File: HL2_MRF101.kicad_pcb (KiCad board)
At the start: 4 copper layers, 149.9 x 100 mm, 224 parts, among them J1 Antenna, J10 DB1, J2 HL2, J3 RF3, J4 RF1, J5 RCJ-041, J6 50VDC, J7 12V, J8 Fan, J9 HL2_12V, K1 EC2-3NU, K10 EC2-3NU, K11 EC2-3NU, K12 EC2-3NU, K13 EC2-3NU, K2 EC2-3NU, K3 EC2-3NU, K4 EC2-3NU, K5 EC2-3NU, K6 EC2-3NU, K7 EC2-3NU, K8 EC2-3NU, K9 EC2-3NU, Q1 MRF101AN, Q2 2N7002, Q3 IRLML6402, Q4 DTC144E, T1 Coupler, T2 Coupler, T3 744851330, U1 MCP6282E/MS, U2 MAX11613, U3 MCP23008, U4 ULN2003, U5 LM35-NEB, U6 MCP4561, U7 INA193

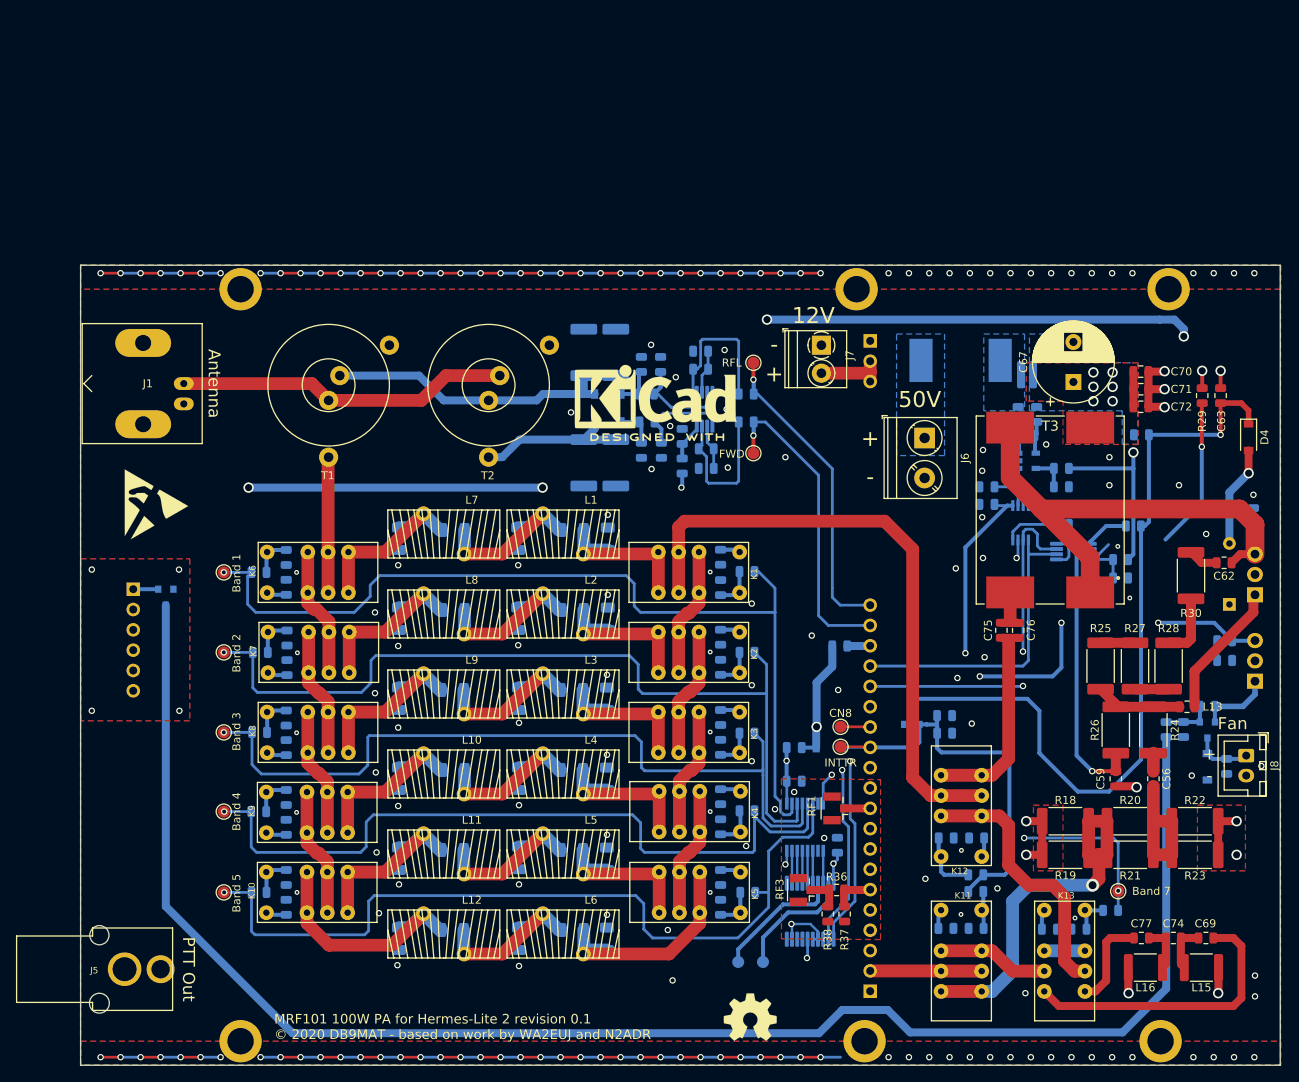
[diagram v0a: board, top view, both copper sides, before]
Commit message: Almost finished reworking FET part
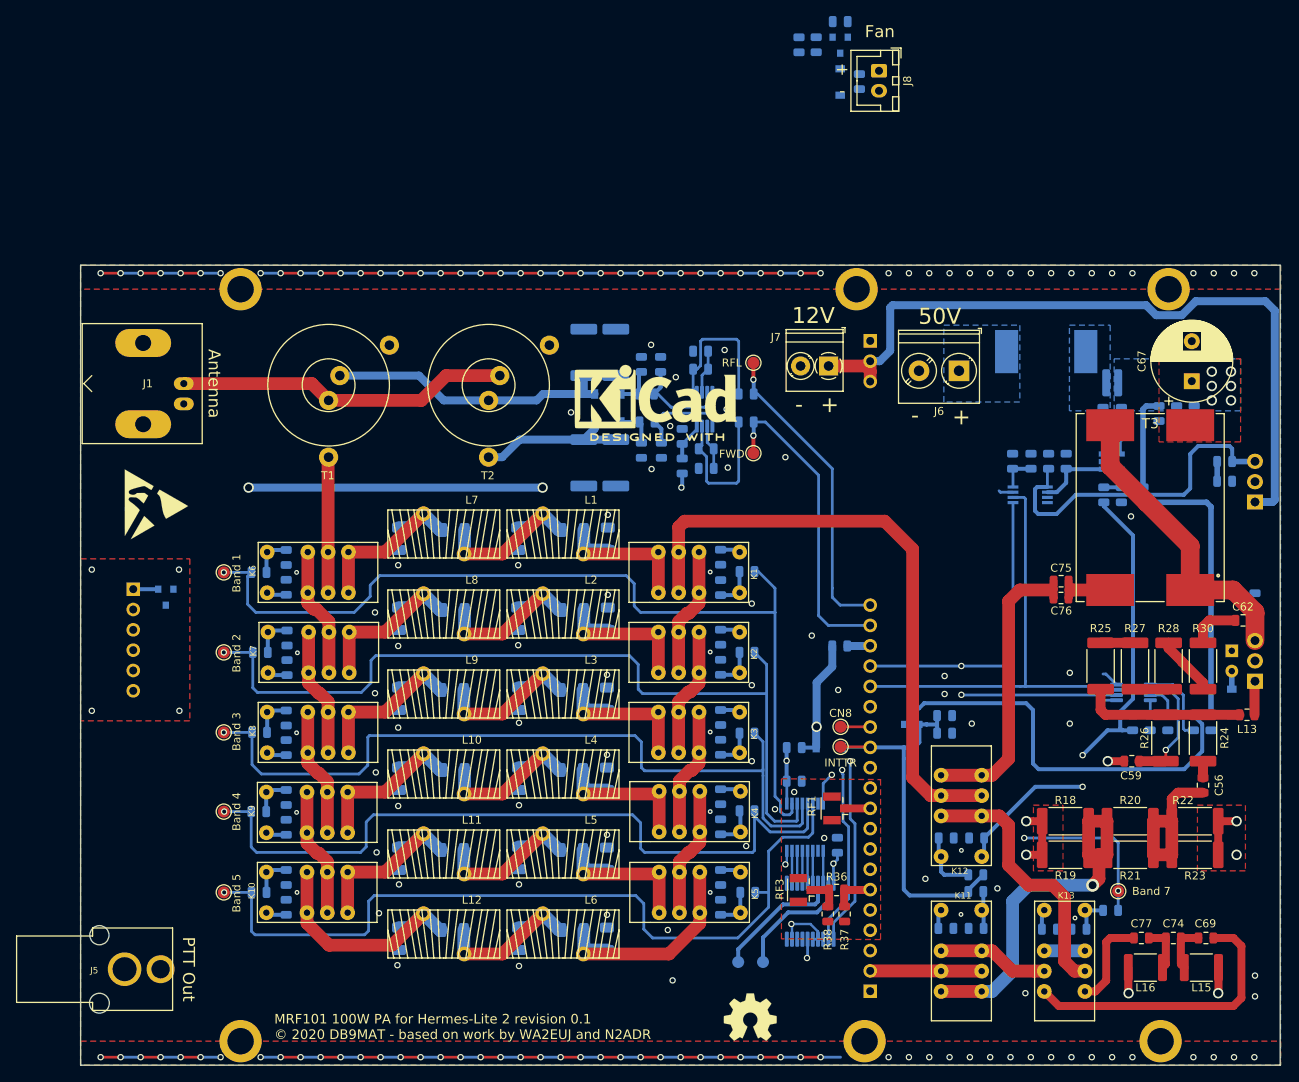
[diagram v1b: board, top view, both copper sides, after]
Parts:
- C63, C70, C71, C72, D4, R29: moved to B.Cu
- D5: footprint Diode_THT:D_DO-35_SOD27_P7.62mm_Horizontal -> Diode_THT:D_DO-35_SOD27_P2.54mm_Vertical_KathodeUp
- moved C85 97.1 mm to (167.3, 17.1)
- moved R16 97.1 mm to (164.9, 9.55)
- moved C84 97.1 mm to (161.9, 12.4)
- moved D6 97.1 mm to (164.9, 17.1)
- moved Q3 97.1 mm to (164.9, 12.5)
- moved J8 97.1 mm to (169.8, 15.7)
- moved R17 97.1 mm to (159.8, 12.4)
- moved R29 41.1 mm to (205.9, 97.2), turned to 90 degrees
- moved C63 40.9 mm to (211.3, 97.2), turned to 90 degrees
- moved D4 33.2 mm to (213.9, 94.7), turned to 90 degrees
- moved R39 25.7 mm to (209.1, 97.2), turned to 270 degrees
- moved C61 22.4 mm to (213.0, 67.0)
- moved U5 22.4 mm to (216.8, 69.6)
- moved R33 22.4 mm to (213.0, 64.5)
- moved FB7 20.5 mm to (201.5, 97.2), turned to 270 degrees
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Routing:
- net Net-(Q4-Pad3): track 205.3 -> 0.00 mm
- net +3V3: track 536.7 -> 459.4 mm, vias 9 -> 8
- net +12V: track 18.0 -> 92.6 mm
- net Vtemp: track 68.6 -> 42.1 mm, vias 4 -> 0
- net SCL: track 75.2 -> 97.3 mm, vias 1 -> 3
- net Net-(C62-Pad1): track 63.0 -> 41.6 mm
- net GND: track 236.2 -> 215.1 mm, vias 204 -> 186
- net Net-(C59-Pad1): track 35.3 -> 15.7 mm
- net Net-(R29-Pad2): track 21.8 -> 4.30 mm, vias 1 -> 0
- net Net-(L13-Pad2): track 17.0 -> 4.23 mm
- net SDA: track 79.9 -> 91.4 mm, vias 3 -> 1
- net TX_high: track 26.1 -> 36.8 mm
- net Net-(D4-Pad2): track 12.6 -> 2.26 mm, vias 1 -> 0
- net Net-(C63-Pad2): track 99.1 -> 89.4 mm, vias 1 -> 0
- net Net-(L13-Pad1): track 10.9 -> 20.2 mm
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
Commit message: Updated FET circuit
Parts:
- R10, R5: value 56k -> 100k
- R11, R4: value 100k -> 56k
- U2: value MAX11613 -> MAX11645
- moved J8 137.4 mm to (74.2, 114.4), turned to 90 degrees
- moved C85 131.9 mm to (76.8, 113.0)
- moved R16 130.4 mm to (76.1, 105.1), turned to 90 degrees
- moved Q3 130.4 mm to (73.2, 105.1), turned to 180 degrees
- moved D6 128.6 mm to (79.2, 112.9)
- moved C84 126.1 mm to (73.2, 102.1), turned to 0 degrees
- moved R17 123.1 mm to (73.2, 99.9), turned to 180 degrees
- moved Q4 17.2 mm to (73.2, 97.0)
- moved C78 2.30 mm to (186.5, 64.5)
- moved FB4 2.30 mm to (188.8, 64.5), turned to 90 degrees
- moved U2 0.33 mm to (188.7, 69.0)
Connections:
- C79 pad 2: Vipa -> Vtemp
- C80 pad 2: Vtemp -> Vipa
- U2 pad 1: Vtemp -> Vipa
- U2 pad 2: Vipa -> Vtemp
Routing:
- net +12V: track 92.6 -> 263.5 mm
- net Net-(J10-Pad1): track 3.12 -> 18.1 mm
- net +3V3: track 459.4 -> 474.3 mm
- net Net-(C85-Pad2): track 0.00 -> 13.9 mm
- net GND: track 215.1 -> 226.5 mm, vias 186 -> 200
- net Net-(C84-Pad2): track 0.00 -> 6.16 mm
- net Vtemp: track 42.1 -> 36.0 mm
- net Net-(Q4-Pad3): track 0.00 -> 2.27 mm
- net Vipa: track 9.30 -> 11.0 mm
- net Net-(C78-Pad2): track 4.56 -> 5.71 mm
- net SDA: track 91.4 -> 90.8 mm
- net Net-(C63-Pad2): track 89.4 -> 88.8 mm

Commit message: Revision 0.2
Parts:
- removed the REF** at (141.9, 56.4)
- added G***: LOGO, n2adr:Ham_Logo, F.Cu at (139.4, 56.2)
- Q3, Q4: footprint TO_SOT_Packages_SMD:SOT-23 -> Package_TO_SOT_SMD:SOT-23
- moved C42 3.16 mm to (94.7, 119.5)
- moved C53 3.16 mm to (94.7, 123.3)
- moved FB18 3.16 mm to (91.3, 121.4)
- moved K10 3.16 mm to (97.3, 121.4)
- moved TP12 3.16 mm to (86.9, 121.4)
- moved C30 3.13 mm to (115.6, 126.1)
- moved L12 3.13 mm to (114.5, 126.6)
- moved C36 3.13 mm to (108.9, 127.2)
- moved C11 3.00 mm to (135.8, 127.2)
- moved C17 3.00 mm to (131.5, 126.1)
- moved C24 3.00 mm to (124.8, 127.2)
- moved L6 3.00 mm to (130.3, 126.6)
- moved C52 2.90 mm to (150.0, 119.4)
- moved C5 2.90 mm to (150.0, 123.2)
- moved FB17 2.90 mm to (153.4, 121.3)
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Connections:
- C79 pad 2: Vtemp -> Vipa
- C80 pad 2: Vipa -> Vtemp
- U2 pad 1: Vipa -> Vtemp
- U2 pad 2: Vtemp -> Vipa
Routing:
- net +3V3: track 474.3 -> 486.2 mm, vias 8 -> 7
- net Band2: track 107.0 -> 111.6 mm
- net Band1: track 114.7 -> 117.8 mm
- net Band3: track 98.6 -> 101.6 mm
- net Vipa: track 11.0 -> 13.1 mm
- net Band5: track 101.8 -> 103.5 mm
- net Net-(TP5-Pad1): track 16.3 -> 17.8 mm
- net Net-(TP2-Pad1): track 15.3 -> 16.7 mm
- net Net-(C63-Pad2): track 88.8 -> 89.9 mm
- net Net-(C16-Pad2): track 21.6 -> 22.5 mm
- net Net-(D2-Pad2): track 39.8 -> 40.7 mm
- net Net-(D1-Pad2): track 19.6 -> 20.5 mm
- net Net-(C13-Pad2): track 21.9 -> 22.8 mm
- net Net-(J1-Pad1): track 41.7 -> 40.8 mm
- net Net-(C17-Pad2): track 21.8 -> 22.7 mm
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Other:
- board text added: "MRF101 100W PA for Hermes-Lite 2 revision 0.2 © 2020 DB9MAT - based on work by WA2EUJ and N2ADR"
- board text removed: "JLCJLCJLCJLC"
- board text removed: "MRF101 100W PA for Hermes-Lite 2 revision 0.1 © 2020 DB9MAT - based on work by WA2EUJ and N2ADR"

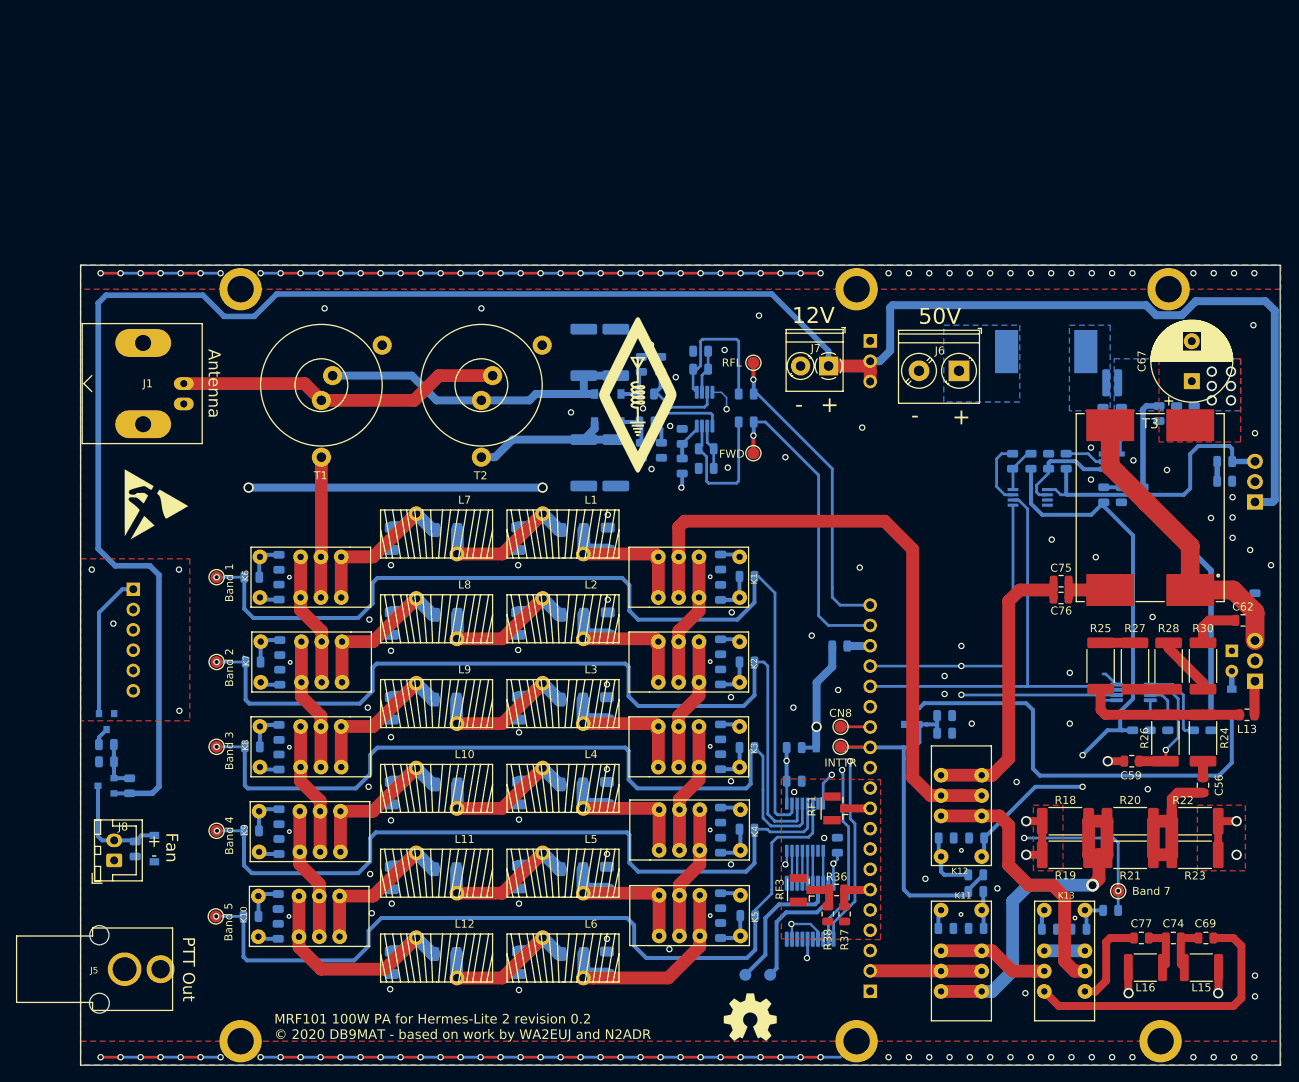
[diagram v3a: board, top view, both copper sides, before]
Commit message: Rx antenna change
RX antenna routed through HL2 rx antenna connection. High power tx tracks thickened to 2 mm and net list added for 50 ohm impedance top and bottom tracks for clearance.
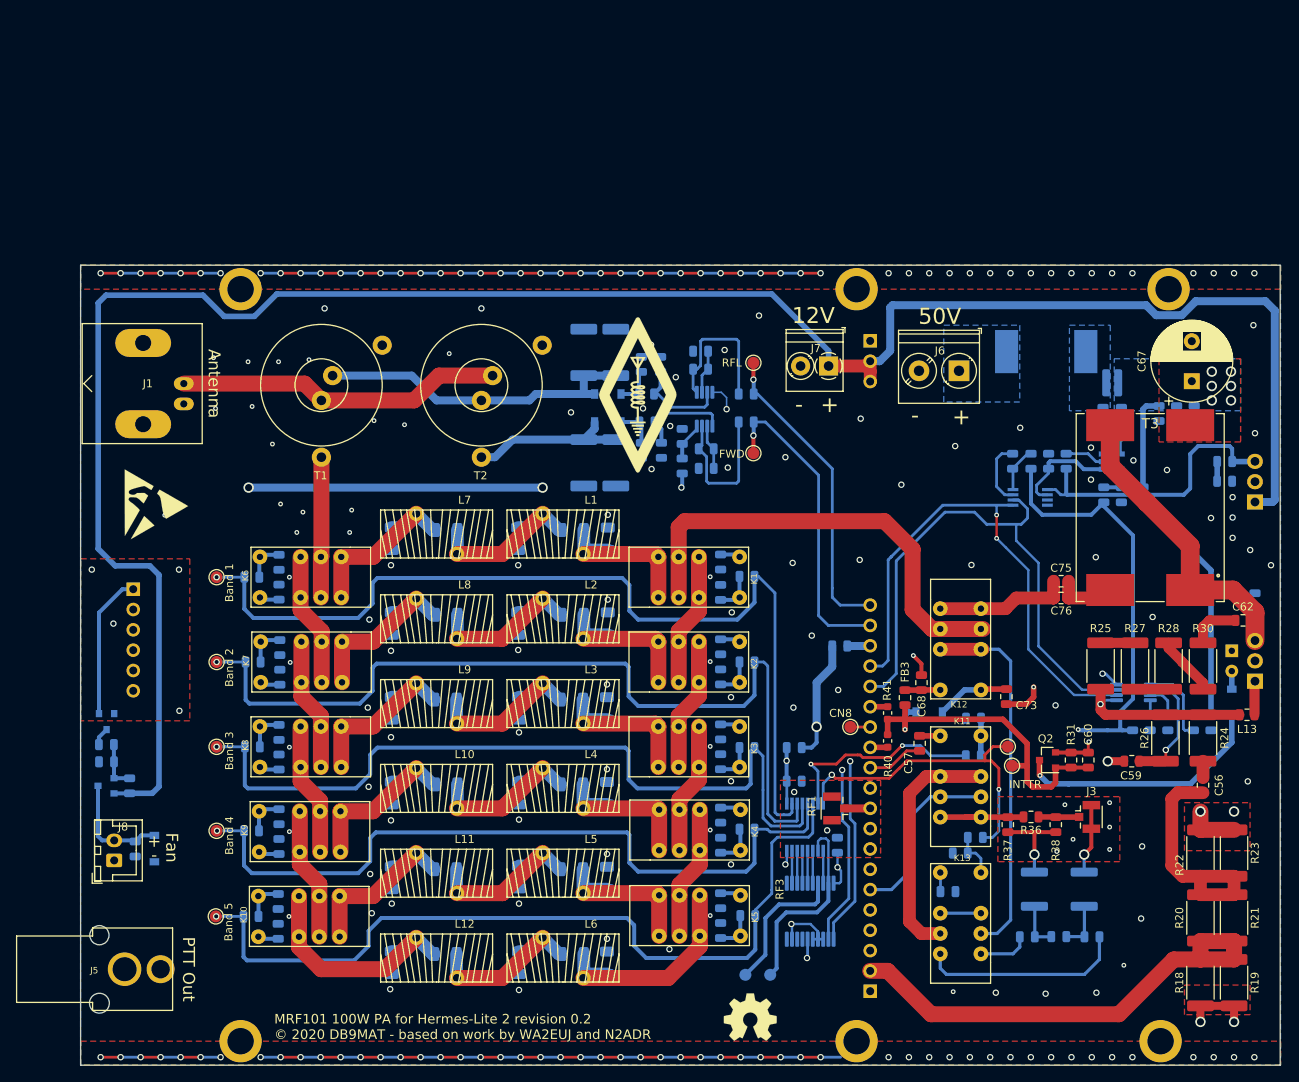
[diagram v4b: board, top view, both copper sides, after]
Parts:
- added R40: 0R, Resistor_SMD:R_0603_1608Metric, F.Cu at (170.9, 99.5)
- added R41: 0R, Resistor_SMD:R_0603_1608Metric, F.Cu at (170.9, 96.0)
- C57, C60, C68, C73, FB3, Q2, R31: moved to F.Cu
- C69, C74, C77, L15, L16: moved to B.Cu
- J3: footprint Connector_Coaxial:U.FL_Hirose_U.FL-R-SMT-1_Vertical -> n2adr:U.FL_Hirose_U.FL-R-SMT-1_Vertical
- moved J3 36.8 mm to (195.9, 109.0), turned to 0 degrees
- moved R38 30.6 mm to (191.9, 109.9)
- moved R19 26.5 mm to (214.2, 129.7), turned to 90 degrees
- moved R18 26.3 mm to (210.0, 129.7), turned to 90 degrees
- moved C58 26.3 mm to (181.6, 96.6)
- moved R36 26.0 mm to (188.8, 109.0), turned to 180 degrees
- moved FB3 23.8 mm to (173.1, 94.1), turned to 90 degrees
- moved C57 23.4 mm to (174.9, 99.8), turned to 270 degrees
- moved R37 23.3 mm to (185.9, 109.9)
- moved TP14 22.7 mm to (185.9, 100.2)
- moved K11 21.8 mm to (180.0, 103.9)
- moved TP7 21.6 mm to (186.4, 102.6)
- moved K12 20.8 mm to (180.0, 88.0)
- moved C68 19.7 mm to (175.1, 92.2), turned to 90 degrees
- moved FB19 19.2 mm to (181.8, 111.5)
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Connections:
- FB2 pad 2: INTTR -> RXANT
- J2 pad 13: INTTR -> Net-(J2-Pad13)
- J2 pad 6: Net-(J2-Pad6) -> HL2_RX
- K11 pad 3: HL2_RF -> HL2_RX
- K11 pad 4: HL2_TX -> Net-(K11-Pad4)
- K11 pad 5: HL2_TX -> Net-(K11-Pad4)
- K11 pad 6: HL2_RF -> HL2_RX
- R18 pad 2: HL2_TX -> HL2_RF
- R19 pad 2: HL2_TX -> HL2_RF
- R20 pad 1: HL2_TX -> HL2_RF
- R21 pad 2: HL2_TX -> HL2_RF
- R36 pad 2: Net-(J2-Pad6) -> Net-(K11-Pad4)
- R37 pad 2: Net-(J2-Pad6) -> Net-(K11-Pad4)
- U4 pad 15: Net-(U4-Pad15) -> RXANT
- U4 pad 2: Net-(U4-Pad2) -> Net-(TP2-Pad1)
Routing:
- net HL2_TX: track 46.7 -> 0.00 mm, vias 1 -> 0
- net HL2_RF: track 14.0 -> 59.4 mm
- net GND: track 226.5 -> 260.3 mm, vias 208 -> 232
- net RXANT: track 0.00 -> 26.4 mm, vias 0 -> 2
- net Net-(C63-Pad2): track 89.9 -> 66.8 mm, vias 0 -> 1
- net HL2_RX: track 0.00 -> 22.7 mm
- net Filter_In: track 77.9 -> 57.2 mm
- net TX_high: track 36.8 -> 16.8 mm
- net Net-(K11-Pad2): track 14.0 -> 30.3 mm
- net SDA: track 90.8 -> 105.1 mm
- net Band7: track 53.3 -> 40.6 mm, vias 3 -> 2
- net Net-(K12-Pad2): track 33.6 -> 46.2 mm
- net Net-(K11-Pad4): track 0.00 -> 12.3 mm
- net Net-(C69-Pad2): track 36.2 -> 25.7 mm
- net Net-(C56-Pad2): track 20.0 -> 29.7 mm
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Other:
- net class 50z_bottom added: clearance 0.5, trace_width 0.4, via_dia 0.6, via_drill 0.3
- net class 50z_top added: clearance 0.5, trace_width 2, via_dia 0.6, via_drill 0.3

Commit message: Update relays
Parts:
- removed the REF** at (153.7, 134.0) (x2)
- removed TP10, TP11, TP12, TP14, TP2, TP8, TP9: P8, TestPoint:TestPoint_Pad_D1.5mm
- added REF**: OSHW-Symbol_6.7x6mm_SilkScreen, Symbol:OSHW-Symbol_6.7x6mm_SilkScreen, B.Cu at (161.0, 133.9)
- added REF**: OSHW-Symbol_6.7x6mm_SilkScreen, Symbol:OSHW-Symbol_6.7x6mm_SilkScreen, F.Cu at (161.2, 133.3)
- C55, D3, FB5: moved to F.Cu
- J10: footprint Connector_PinSocket_2.54mm:PinSocket_1x06_P2.54mm_Vertical -> Connector_PinHeader_2.54mm:PinHeader_1x06_P2.54mm_Vertical
- J4: footprint Connector_Coaxial:U.FL_Hirose_U.FL-R-SMT-1_Vertical -> n2adr:U.FL_Hirose_U.FL-R-SMT-1_Vertical
- K1, K10, K12, K2, K3, K4, K5, K6, K7, K8, K9: value EC2-3NU -> AXICOM D2N; footprint n2adr:RelayDPDT01 -> n2adr:RelayDPDT02
- moved D3 15.7 mm to (191.6, 98.0)
- moved TP5 11.4 mm to (164.5, 129.5)
- moved FB5 7.75 mm to (159.8, 108.0), turned to 90 degrees
- moved C53 7.68 mm to (88.1, 127.3)
- moved C38 7.37 mm to (87.9, 74.6)
- moved C51 7.30 mm to (88.1, 115.6)
- moved C39 7.18 mm to (87.9, 86.3)
- moved C46 7.04 mm to (87.9, 92.1)
- moved C44 6.93 mm to (87.9, 80.4)
- moved C42 6.87 mm to (88.1, 121.6)
- moved C49 6.85 mm to (88.1, 103.7)
- moved C41 6.73 mm to (88.1, 109.9)
- moved C40 6.68 mm to (88.1, 98.0)
- moved FB17 6.29 mm to (154.4, 127.5), turned to 90 degrees
- moved FB15 5.27 mm to (154.4, 115.6), turned to 90 degrees
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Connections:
- C43 pad 2: +3V3 -> +12V
- C44 pad 2: +3V3 -> +12V
- C45 pad 2: +3V3 -> +12V
- C46 pad 2: +3V3 -> +12V
- C48 pad 2: +3V3 -> +12V
- C49 pad 2: +3V3 -> +12V
- C50 pad 2: +3V3 -> +12V
- C51 pad 2: +3V3 -> +12V
- C52 pad 2: +3V3 -> +12V
- C53 pad 2: +3V3 -> +12V
- C54 pad 2: Net-(C54-Pad2) -> +3V3
- C55 pad 2: Net-(C54-Pad2) -> Net-(C55-Pad2)
- C57 pad 1: +3V3 -> +12V
- C65 pad 2: +3V3 -> +12V
- C73 pad 1: +3V3 -> +12V
- FB5 pad 1: +3V3 -> +12V
- FB5 pad 2: Net-(C54-Pad2) -> Net-(C55-Pad2)
- K1 pad 1: +3V3 -> +12V
- K10 pad 1: +3V3 -> +12V
- K11 pad 1: +3V3 -> +12V
- K12 pad 1: +3V3 -> +12V
- K13 pad 1: +3V3 -> +12V
- K2 pad 1: +3V3 -> +12V
- K3 pad 1: +3V3 -> +12V
- K4 pad 1: +3V3 -> +12V
- K5 pad 1: +3V3 -> +12V
- K6 pad 1: +3V3 -> +12V
- K7 pad 1: +3V3 -> +12V
- K8 pad 1: +3V3 -> +12V
- K9 pad 1: +3V3 -> +12V
- U3 pad 20: Net-(C54-Pad2) -> +3V3
- U4 pad 9: Net-(C54-Pad2) -> Net-(C55-Pad2)
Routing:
- net +3V3: track 478.8 -> 194.1 mm, vias 6 -> 8
- net +12V: track 263.5 -> 524.3 mm
- net GND: track 260.3 -> 308.7 mm, vias 232 -> 222
- net Net-(C54-Pad2): track 27.8 -> 0.00 mm, vias 2 -> 0
- net Band2: track 111.6 -> 86.7 mm, vias 1 -> 0
- net Band3: track 101.6 -> 78.6 mm, vias 1 -> 2
- net Band4: track 95.2 -> 77.4 mm, vias 1 -> 0
- net Net-(U3-Pad19): track 24.8 -> 8.06 mm
- net Band1: track 117.8 -> 102.5 mm, vias 1 -> 2
- net Band5: track 103.5 -> 92.1 mm, vias 1 -> 2
- net Net-(K12-Pad2): track 46.2 -> 56.1 mm
- net Net-(C30-Pad2): track 30.7 -> 39.0 mm
- net Net-(C55-Pad2): track 0.00 -> 6.36 mm, vias 0 -> 1
- net Net-(K3-Pad2): track 16.5 -> 22.0 mm
- net Net-(K10-Pad3): track 16.7 -> 22.0 mm
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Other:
- board text added: "MRF101 100W PA for Hermes-Lite 2 r0.3 © 2020 DB9MAT (mods M5EVT) - based on work by WA2EUJ+N2ADR"
- board text removed: "Band 1"
- board text removed: "Band 2"
- board text removed: "Band 3"
- board text removed: "Band 4"
- board text removed: "Band 5"
- board text removed: "MRF101 100W PA for Hermes-Lite 2 revision 0.2 © 2020 DB9MAT - based on work by WA2EUJ and N2ADR"
